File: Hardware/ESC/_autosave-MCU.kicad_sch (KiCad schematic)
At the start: 27 parts, among them J3 GPIO_Connections, Y1 Crystal_GND24

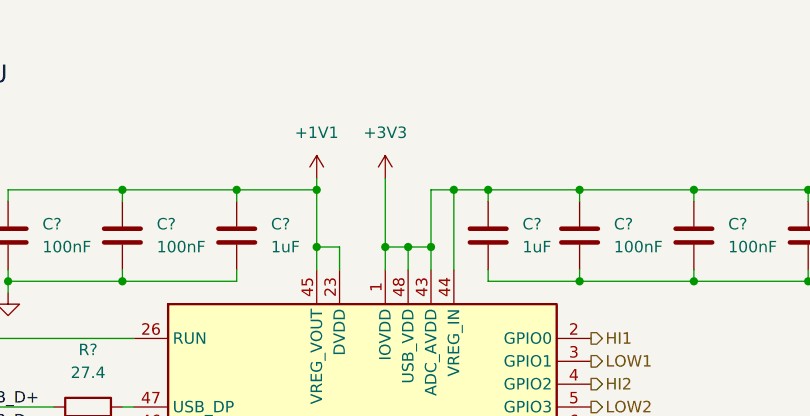
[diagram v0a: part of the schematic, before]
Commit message: Breaking + BEMF ZCD Detector
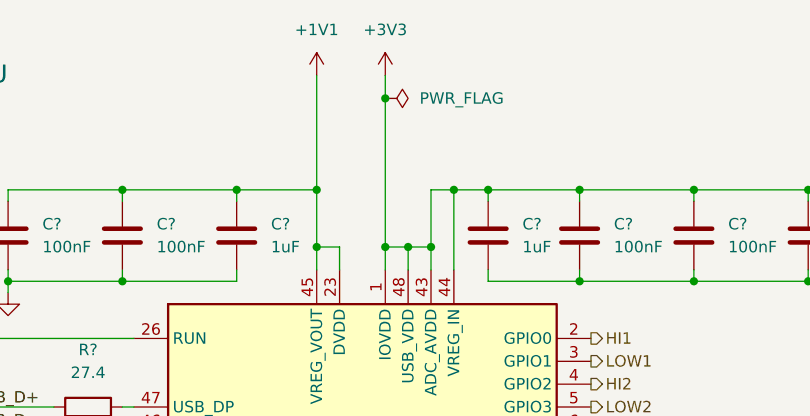
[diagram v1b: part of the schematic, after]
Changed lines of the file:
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@@
   (junction (at 237.49 147.32) (diameter 0) (color 0 0 0 0)
+  )
+  (junction (at 76.2 25.4) (diameter 0) (color 0 0 0 0)
   )
   (junction (at 267.97 91.44) (diameter 0) (color 0 0 0 0)
@@
     (stroke (width 0) (type default))
   )
-  (wire (pts (xy 68.58 34.29) (xy 68.58 35.56))
+  (wire (pts (xy 68.58 22.86) (xy 68.58 35.56))
     (stroke (width 0) (type default))
   )
@@
     (stroke (width 0) (type default))
   )
-  (wire (pts (xy 76.2 34.29) (xy 76.2 41.91))
+  (wire (pts (xy 76.2 22.86) (xy 76.2 25.4))
     (stroke (width 0) (type default))
   )
@@
   )
   (wire (pts (xy 73.66 137.16) (xy 73.66 140.97))
+    (stroke (width 0) (type default))
+  )
+  (wire (pts (xy 76.2 25.4) (xy 76.2 41.91))
     (stroke (width 0) (type default))
   )
@@
     )
   )
-  (symbol (lib_id "power:+3V3") (at 76.2 34.29 0) (unit 1)
+  (symbol (lib_id "power:+3V3") (at 76.2 22.86 0) (unit 1)
     (in_bom yes) (on_board yes) (dnp no)
-    (property "Reference" "#PWR?" (at 76.2 38.1 0)
-      (effects (font (size 1.27 1.27)) hide)
-    )
-    (property "Value" "+3V3" (at 76.2 29.21 0)
-      (effects (font (size 1.27 1.27)))
-    )
-    (property "Footprint" "" (at 76.2 34.29 0)
-      (effects (font (size 1.27 1.27)) hide)
-    )
-    (property "Datasheet" "" (at 76.2 34.29 0)
+    (property "Reference" "#PWR?" (at 76.2 26.67 0)
+      (effects (font (size 1.27 1.27)) hide)
+    )
+    (property "Value" "+3V3" (at 76.2 17.78 0)
+      (effects (font (size 1.27 1.27)))
+    )
+    (property "Footprint" "" (at 76.2 22.86 0)
+      (effects (font (size 1.27 1.27)) hide)
+    )
+    (property "Datasheet" "" (at 76.2 22.86 0)
       (effects (font (size 1.27 1.27)) hide)
     )
@@
     )
   )
-  (symbol (lib_id "power:+1V1") (at 68.58 34.29 0) (unit 1)
-    (in_bom yes) (on_board yes) (dnp no) (fields_autoplaced)
-    (property "Reference" "#PWR?" (at 68.58 38.1 0)
-      (effects (font (size 1.27 1.27)) hide)
-    )
-    (property "Value" "+1V1" (at 68.58 29.21 0)
-      (effects (font (size 1.27 1.27)))
-    )
-    (property "Footprint" "" (at 68.58 34.29 0)
-      (effects (font (size 1.27 1.27)) hide)
-    )
-    (property "Datasheet" "" (at 68.58 34.29 0)
-      (effects (font (size 1.27 1.27)) hide)
-    )
+  (symbol (lib_id "power:PWR_FLAG") (at 76.2 25.4 270) (unit 1)
+    (in_bom yes) (on_board yes) (dnp no)
+    (property "Reference" "#FLG04" (at 78.105 25.4 0)
+      (effects (font (size 1.27 1.27)) hide)
+    )
+    (property "Value" "PWR_FLAG" (at 80.01 25.4 90)
+      (effects (font (size 1.27 1.27)) (justify left))
+    )
+    (property "Footprint" "" (at 76.2 25.4 0)
+      (effects (font (size 1.27 1.27)) hide)
+    )
+    (property "Datasheet" "~" (at 76.2 25.4 0)
+      (effects (font (size 1.27 1.27)) hide)
+    )
+    (pin "1")
+    (instances
+      (project "BLDC_ESC"
+        (path "/bd67e774-828f-47d6-928d-7f9ad42d6cab/dac7d52f-093d-43cb-8a30-f6f652ecb1a6"
+          (reference "#FLG04") (unit 1)
+        )
+        (path "/bd67e774-828f-47d6-928d-7f9ad42d6cab/0bf7d76f-f99b-4503-84a3-7b4d4ee9922c"
+          (reference "#FLG02") (unit 1)
+        )
+      )
+    )
+  )
+  (symbol (lib_id "power:+1V1") (at 68.58 22.86 0) (unit 1)
+    (in_bom yes) (on_board yes) (dnp no) (fields_autoplaced)
+    (property "Reference" "#PWR?" (at 68.58 26.67 0)
+      (effects (font (size 1.27 1.27)) hide)
+    )
+    (property "Value" "+1V1" (at 68.58 17.78 0)
+      (effects (font (size 1.27 1.27)))
+    )
+    (property "Footprint" "" (at 68.58 22.86 0)
+      (effects (font (size 1.27 1.27)) hide)
+    )
+    (property "Datasheet" "" (at 68.58 22.86 0)
+      (effects (font (size 1.27 1.27)) hide)
+    )
